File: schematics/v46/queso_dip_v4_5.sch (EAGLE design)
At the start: 50 parts, among them Q1 FOXSDLF/120-20, U1 PRTR5V0U2X,215, U2 PRTR5V0U2X,215, U3 PRTR5V0U2X,215, U4 PRTR5V0U2X,215, U5 PRTR5V0U2X,215, X1 USB-A-HU, X2 USB-A-HU, X3 USB-A-HU, X4 USB-A-HU

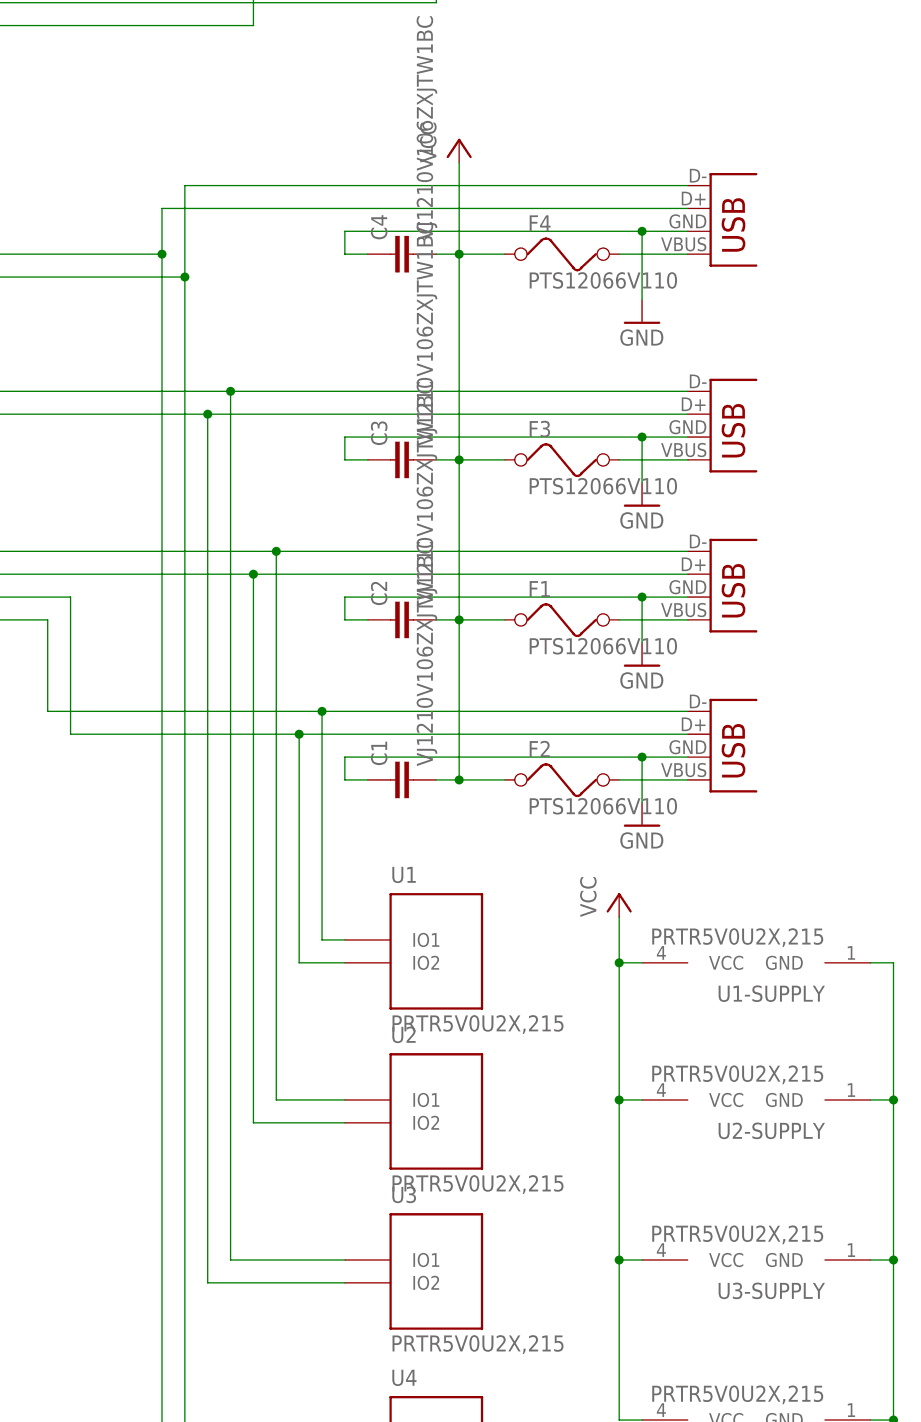
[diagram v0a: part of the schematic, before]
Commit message: added flat usb version
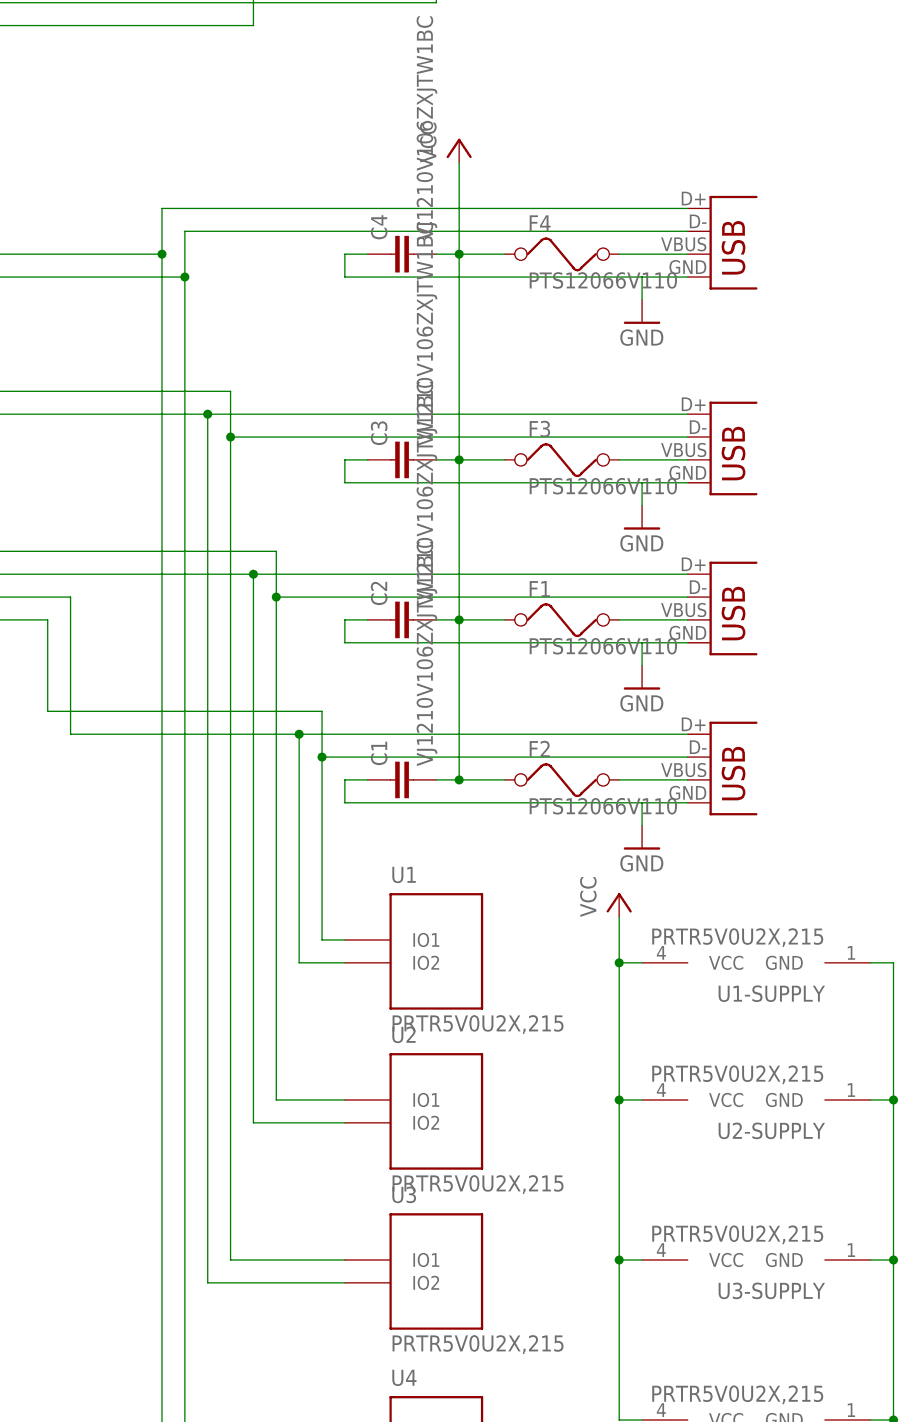
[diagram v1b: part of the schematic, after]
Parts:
- X1, X2, X3, X4: value USB-A-HU -> USB-A-S; device con-usb:USB-A-HU -> con-usb:USB-A-S
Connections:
- net DM1: now also X4.D-; no longer X4.D+
- net DM2: now also X3.D-; no longer X3.D+
- net DM3: now also X2.D-; no longer X2.D+
- net DM4: now also X1.D-; no longer X1.D+
- net DP1: now also X4.D+; no longer X4.D-
- net DP2: now also X3.D+; no longer X3.D-
- net DP3: now also X2.D+; no longer X2.D-
- net DP4: now also X1.D+; no longer X1.D-
- net GND: now also X1.GND, X2.GND, X3.GND, X4.GND; no longer X1.VBUS, X2.VBUS, X3.VBUS, X4.VBUS
- net N$1: now also X1.VBUS; no longer X1.GND
- net N$3: now also X4.VBUS; no longer X4.GND
- net N$4: now also X2.VBUS; no longer X2.GND
- net N$5: now also X3.VBUS; no longer X3.GND
